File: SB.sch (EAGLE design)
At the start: 50 parts, among them IC1 ATMEGA32U4NT-TQFP, IC2 HX711-SOP16L, J2 RJ12, J3 AUDIO-JACK-PJ321, J5 USB-C-16P-16P, K1 HE721C-DIP, Q1 2N7002, Q2 2N7002, Q3 2N3906, SW1 SWITCH-SPDT-4TABSSMT, SW2 SWITCH-SPDT-4TABSSMT

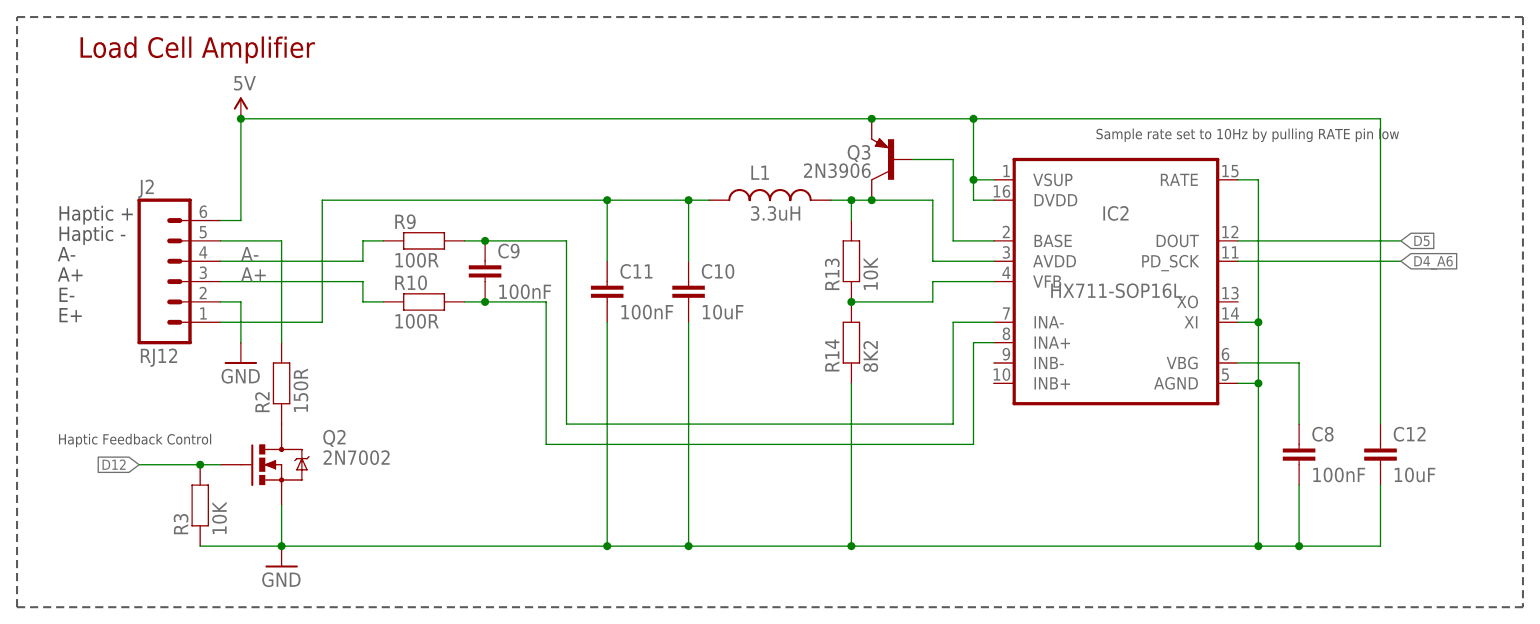
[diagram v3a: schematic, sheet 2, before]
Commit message: Removed haptic feedback and changed to RJ10 connector for v3.0 release
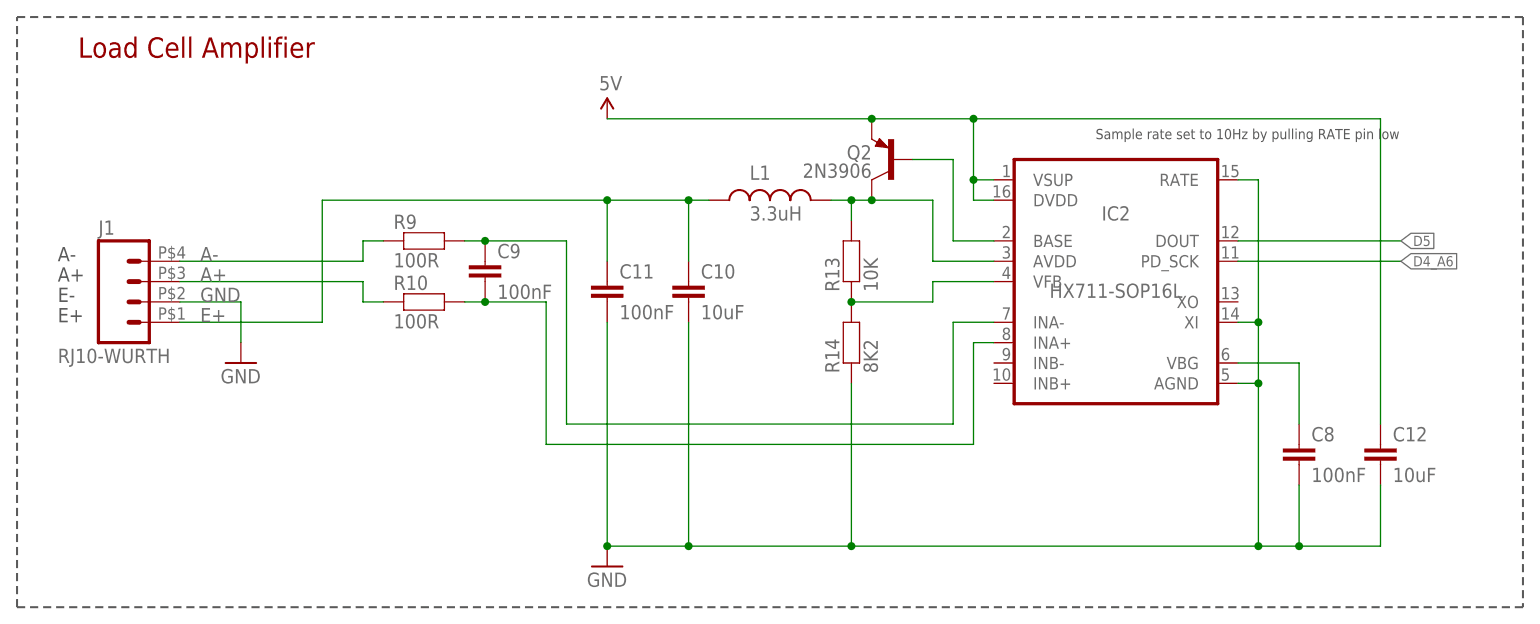
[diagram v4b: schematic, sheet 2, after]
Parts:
- removed J5: USB-C-16P-16P, SuperHouse-Connectors:USB-C-16P-16P
- removed Q3: 2N3906, SuperHouse-DiscreteSemi:TRANS_PNPMMBT3906LT1SOT23-BEC
- removed R12: 22R, SuperHouse-DiscreteSemi:RESISTOR0603
- removed R24: 1K, SuperHouse-DiscreteSemi:RESISTOR0603
- added J1: RJ10-WURTH, SuperHouse-Connectors:RJ10-WURTH
- J2: value RJ12 -> AUDIO-JACK-PJ321; device SuperHouse-Connectors:RJ12 -> SuperHouse-Connectors:AUDIO-JACK-PJ321
- J3: value AUDIO-JACK-PJ321 -> USB-C-16P-16P; device SuperHouse-Connectors:AUDIO-JACK-PJ321 -> SuperHouse-Connectors:USB-C-16P-16P
- Q2: value 2N7002 -> 2N3906; device SuperHouse-DiscreteSemi:MOSFET-NCHANNEL-233 -> SuperHouse-DiscreteSemi:TRANS_PNPMMBT3906LT1SOT23-BEC
- R11: value 22R -> 1K
- R2: value 150R -> 10K
- R3, R4: value 10K -> 5k1
- R5: value 5k1 -> 10K
- R6: value 5k1 -> 4K7
- R7: value 10K -> 22R
- R8: value 4K7 -> 22R
- renumbered LED4 to LED2, S1 to SW3, S2 to SW4, S3 to SW5
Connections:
- removed net N$2: J2.5, R2.2
- removed net N$8: Q2.D, R2.1
- net 5V: now also Q2.E, R2.2, R5.2, R6.2; no longer J2.6, Q3.E, R4.2, R7.2, R8.2
- net A+: now also J1.3; no longer J2.3
- net A-: now also J1.4; no longer J2.4
- net A0: now also R2.1; no longer R4.1
- net D+: now also J3.D+, R8.1; no longer J5.D+, R12.1
- net D-: now also J3.D-, R7.1; no longer J5.D-, R11.1
- net D12: no longer Q2.G, R3.2
- net D13: now also R11.1; no longer R24.1
- net E+: now also J1.1; no longer J2.1
- net GND: now also J1.2, J3.GND, R4.1; no longer J2.2, J5.GND, Q2.S, R5.1, R6.1
- net N$1: now also R11.2; no longer R24.2
- net N$10: now also J3.CC2, R4.2; no longer J5.CC2, R6.2
- net N$13: now also J3.CC1, R3.2; no longer J5.CC1, R5.2
- net N$16: now also Q2.C; no longer Q3.C
- net N$20: now also Q2.B; no longer Q3.B
- net N$5: now also R6.1; no longer R8.1
- net N$7: now also J2.4A, J2.4B; no longer J3.4A, J3.4B
- net N$9: now also J2.3; no longer J3.3
- net RD+: now also R8.2; no longer R12.2
- net RD-: now also R7.2; no longer R11.2
- net RESET: now also R5.1; no longer R7.1
- net USB+: now also J3.VBUS; no longer J5.VBUS
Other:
- note added: "A0: Rotary encoder button (enable SW pull-up) A1: Tare button (enable SW pull-up) D0: Rotary encoder A D1: Rotary encoder B D2: I2C SDA D3: I2C SCL D4: HX711 DOUT D5: HX711 SCK D6: Relay D7: Beep stretch switch (enable SW pull-up) D13: LED"
- note added: "V3.0 (2020-05-08)"
- note removed: "A0: Rotary encoder button (enable SW pull-up) A1: Tare button (enable SW pull-up) D0: Rotary encoder A D1: Rotary encoder B D2: I2C SDA D3: I2C SCL D4: HX711 DOUT D5: HX711 SCK D6: Relay D7: Mode switch D12: Haptic feedback D13: LED"
- note removed: "Haptic +"
- note removed: "Haptic -"
- note removed: "Haptic Feedback Control"
- note removed: "V2.1 (2020-04-23)"
- moved on the sheet: R11, R4, R5, R6, R7, R8

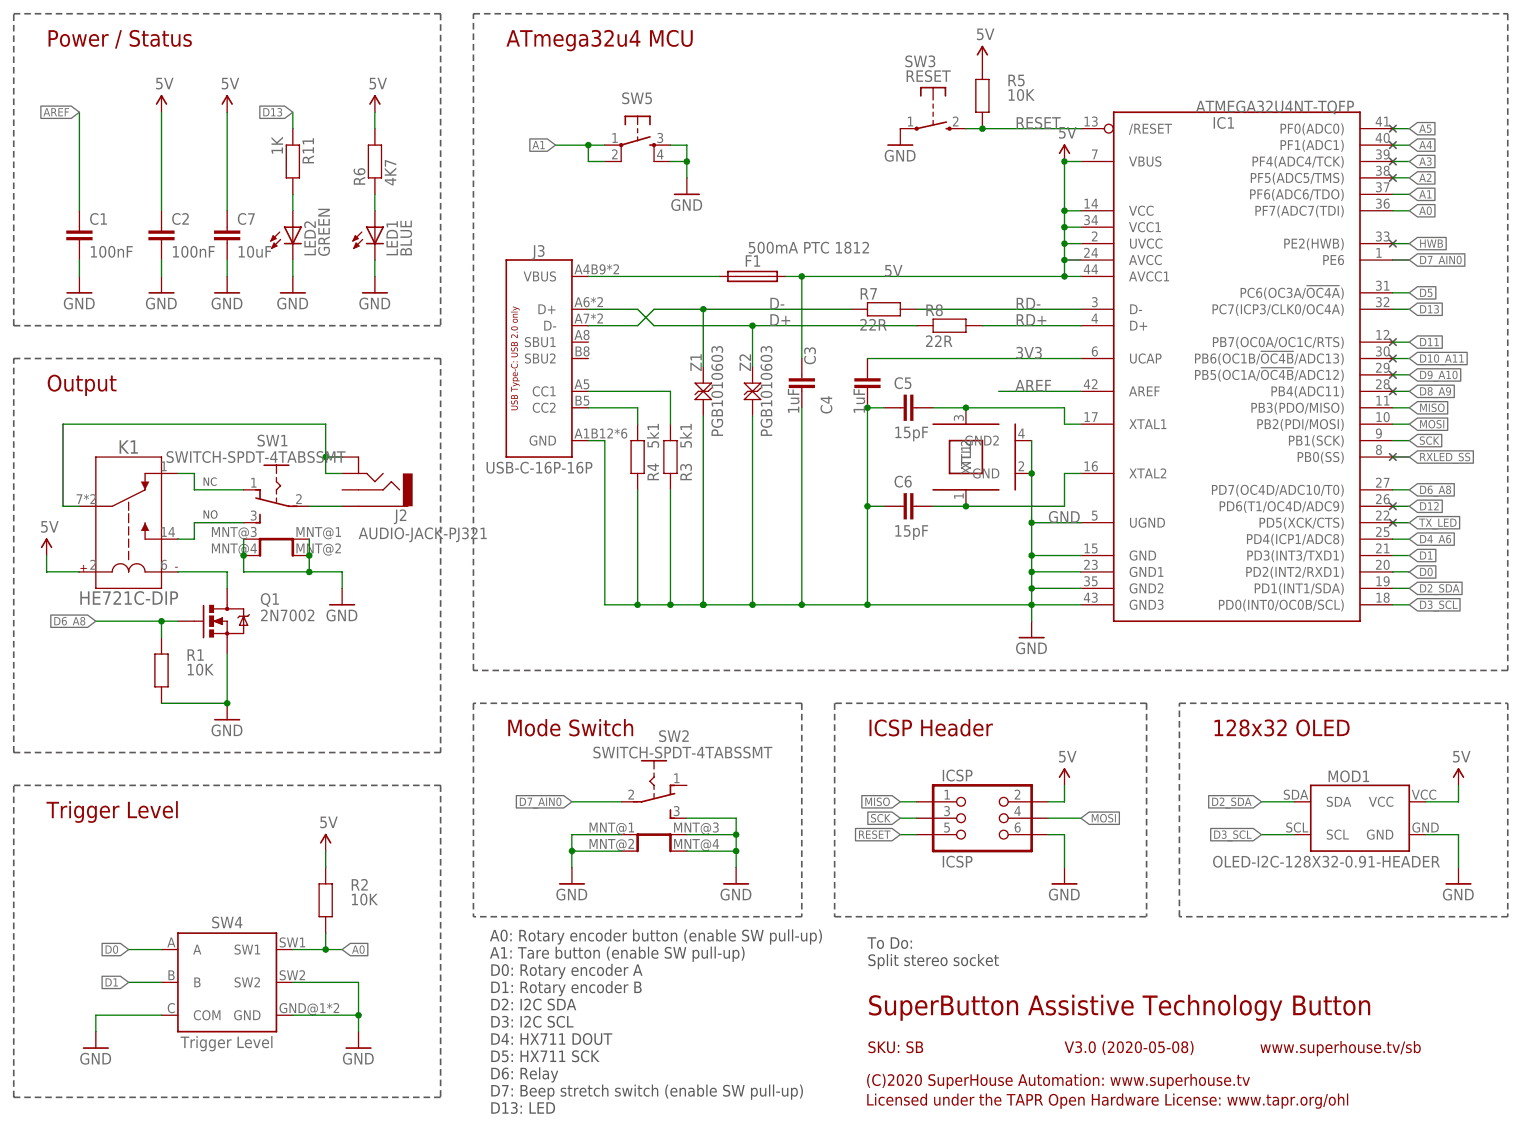
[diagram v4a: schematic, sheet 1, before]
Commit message: Still for v3.0 release: updated design rules and improved clearances
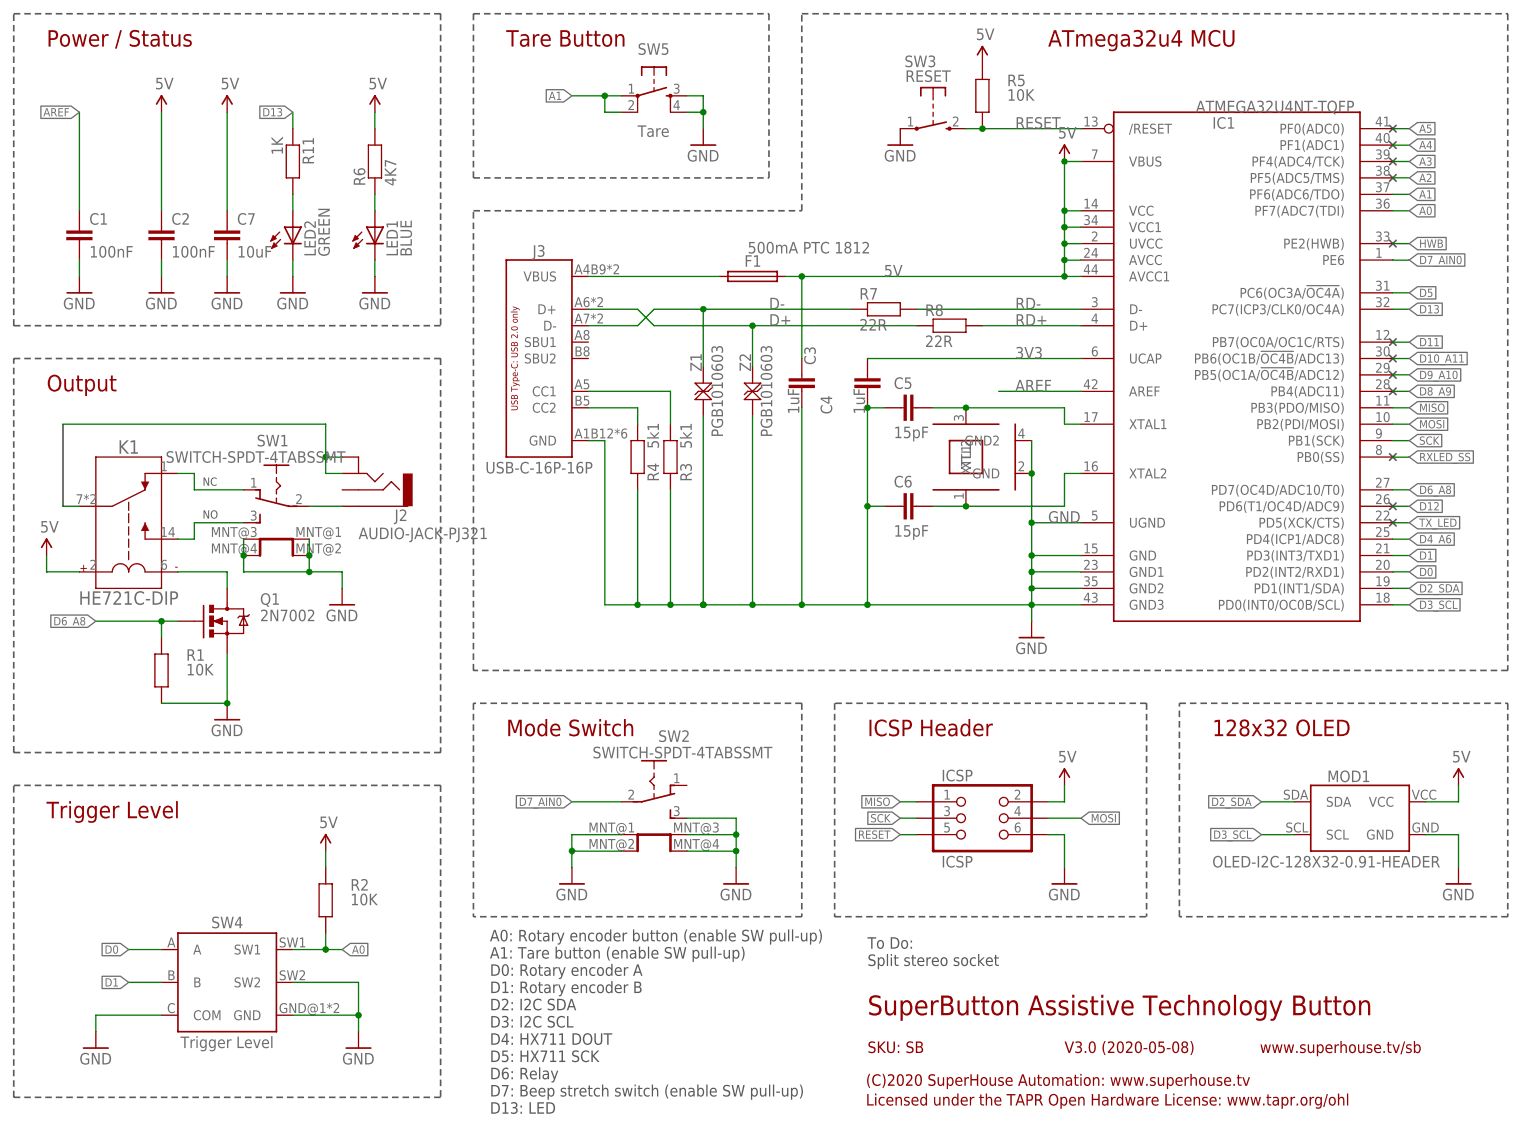
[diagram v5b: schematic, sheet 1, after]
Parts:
- SW5: value (none) -> Tare
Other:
- note added: "Tare Button"
- moved on the sheet: SW5
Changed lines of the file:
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@@
 <part name="GND14" library="SuperHouse-SupplySymbols" library_urn="urn:adsk.eagle:library:11790503" deviceset="GND" device=""/>
 <part name="GND16" library="SuperHouse-SupplySymbols" library_urn="urn:adsk.eagle:library:11790503" deviceset="GND" device=""/>
-<part name="SW5" library="SuperHouse-Switches" library_urn="urn:adsk.eagle:library:11744182" deviceset="TAC_SWITCH" device="-PTH-4.5" package3d_urn="urn:adsk.eagle:package:7066371/2"/>
+<part name="SW5" library="SuperHouse-Switches" library_urn="urn:adsk.eagle:library:11744182" deviceset="TAC_SWITCH" device="-PTH-4.5" package3d_urn="urn:adsk.eagle:package:7066371/2" value="Tare"/>
 <part name="GND17" library="SuperHouse-SupplySymbols" library_urn="urn:adsk.eagle:library:11790503" deviceset="GND" device=""/>
 <part name="J1" library="SuperHouse-Connectors" library_urn="urn:adsk.eagle:library:11765989" deviceset="RJ10" device="-WURTH" package3d_urn="urn:adsk.eagle:package:15628373/2"/>
@@
 <frame x1="0" y1="0" x2="248.92" y2="185.42" columns="8" rows="5" layer="94"/>
 <text x="142.24" y="63.5" size="2.54" layer="94" ratio="12">ICSP Header</text>
-<text x="86.36" y="170.18" size="2.54" layer="94" ratio="12">ATmega32u4 MCU</text>
+<text x="86.36" y="170.18" size="2.54" layer="94" ratio="12">Tare Button</text>
 <text x="142.24" y="20.32" size="3.048" layer="94">SuperButton Assistive Technology Button</text>
 <text x="172.72" y="14.478" size="1.778" layer="94">V3.0 (2020-05-08)</text>
@@
 <wire x1="76.2" y1="127" x2="10.16" y2="127" width="0.254" layer="97" style="longdash"/>
 <wire x1="10.16" y1="127" x2="10.16" y2="175.26" width="0.254" layer="97" style="longdash"/>
-<wire x1="81.28" y1="175.26" x2="241.3" y2="175.26" width="0.254" layer="97" style="longdash"/>
+<wire x1="81.28" y1="175.26" x2="127" y2="175.26" width="0.254" layer="97" style="longdash"/>
+<wire x1="132.08" y1="175.26" x2="241.3" y2="175.26" width="0.254" layer="97" style="longdash"/>
 <wire x1="241.3" y1="175.26" x2="241.3" y2="73.66" width="0.254" layer="97" style="longdash"/>
 <wire x1="241.3" y1="73.66" x2="81.28" y2="73.66" width="0.254" layer="97" style="longdash"/>
-<wire x1="81.28" y1="73.66" x2="81.28" y2="175.26" width="0.254" layer="97" style="longdash"/>
+<wire x1="81.28" y1="73.66" x2="81.28" y2="144.78" width="0.254" layer="97" style="longdash"/>
+<wire x1="81.28" y1="149.86" x2="81.28" y2="175.26" width="0.254" layer="97" style="longdash"/>
 <text x="83.82" y="5.08" size="1.778" layer="97">A0: Rotary encoder button (enable SW pull-up)
 A1: Tare button (enable SW pull-up)
@@
 <wire x1="132.08" y1="35.56" x2="81.28" y2="35.56" width="0.254" layer="97" style="longdash"/>
 <text x="86.36" y="63.5" size="2.54" layer="94" ratio="12">Mode Switch</text>
+<text x="170.18" y="170.18" size="2.54" layer="94" ratio="12">ATmega32u4 MCU</text>
+<wire x1="81.28" y1="144.78" x2="132.08" y2="144.78" width="0.254" layer="97" style="longdash"/>
+<wire x1="81.28" y1="149.86" x2="127" y2="149.86" width="0.254" layer="97" style="longdash"/>
+<wire x1="127" y1="149.86" x2="127" y2="175.26" width="0.254" layer="97" style="longdash"/>
+<wire x1="132.08" y1="144.78" x2="132.08" y2="175.26" width="0.254" layer="97" style="longdash"/>
 </plain>
 <instances>
@@
 <attribute name="VALUE" x="93.98" y="38.1" size="1.778" layer="96"/>
 </instance>
-<instance part="SW5" gate="S" x="106.68" y="154.94" smashed="yes">
-<attribute name="NAME" x="104.14" y="161.29" size="1.778" layer="95"/>
-<attribute name="VALUE" x="104.14" y="148.59" size="1.778" layer="96"/>
-</instance>
-<instance part="GND17" gate="1" x="114.3" y="147.32" smashed="yes">
-<attribute name="VALUE" x="111.76" y="144.78" size="1.778" layer="96"/>
+<instance part="SW5" gate="S" x="109.22" y="162.56" smashed="yes">
+<attribute name="NAME" x="106.68" y="168.91" size="1.778" layer="95"/>
+<attribute name="VALUE" x="106.68" y="156.21" size="1.778" layer="96"/>
+</instance>
+<instance part="GND17" gate="1" x="116.84" y="154.94" smashed="yes">
+<attribute name="VALUE" x="114.3" y="152.4" size="1.778" layer="96"/>
 </instance>
 <instance part="U$14" gate="G$1" x="223.52" y="99.06" smashed="yes"/>
@@
 <segment>
 <pinref part="SW5" gate="S" pin="2"/>
-<wire x1="101.6" y1="152.4" x2="99.06" y2="152.4" width="0.1524" layer="91"/>
-<wire x1="99.06" y1="152.4" x2="99.06" y2="154.94" width="0.1524" layer="91"/>
+<wire x1="104.14" y1="160.02" x2="101.6" y2="160.02" width="0.1524" layer="91"/>
+<wire x1="101.6" y1="160.02" x2="101.6" y2="162.56" width="0.1524" layer="91"/>
 <pinref part="SW5" gate="S" pin="1"/>
-<wire x1="99.06" y1="154.94" x2="101.6" y2="154.94" width="0.1524" layer="91"/>
-<wire x1="99.06" y1="154.94" x2="93.98" y2="154.94" width="0.1524" layer="91"/>
-<junction x="99.06" y="154.94"/>
-<label x="93.98" y="154.94" size="1.27" layer="95" rot="R180" xref="yes"/>
+<wire x1="101.6" y1="162.56" x2="104.14" y2="162.56" width="0.1524" layer="91"/>
+<wire x1="101.6" y1="162.56" x2="96.52" y2="162.56" width="0.1524" layer="91"/>
+<junction x="101.6" y="162.56"/>
+<label x="96.52" y="162.56" size="1.27" layer="95" rot="R180" xref="yes"/>
 </segment>
 </net>
@@
 <pinref part="SW5" gate="S" pin="4"/>
 <pinref part="GND17" gate="1" pin="GND"/>
-<wire x1="111.76" y1="152.4" x2="114.3" y2="152.4" width="0.1524" layer="91"/>
-<wire x1="114.3" y1="152.4" x2="114.3" y2="149.86" width="0.1524" layer="91"/>
+<wire x1="114.3" y1="160.02" x2="116.84" y2="160.02" width="0.1524" layer="91"/>
+<wire x1="116.84" y1="160.02" x2="116.84" y2="157.48" width="0.1524" layer="91"/>
 <pinref part="SW5" gate="S" pin="3"/>
-<wire x1="111.76" y1="154.94" x2="114.3" y2="154.94" width="0.1524" layer="91"/>
-<wire x1="114.3" y1="154.94" x2="114.3" y2="152.4" width="0.1524" layer="91"/>
-<junction x="114.3" y="152.4"/>
+<wire x1="114.3" y1="162.56" x2="116.84" y2="162.56" width="0.1524" layer="91"/>
+<wire x1="116.84" y1="162.56" x2="116.84" y2="160.02" width="0.1524" layer="91"/>
+<junction x="116.84" y="160.02"/>
 </segment>
 </net>
